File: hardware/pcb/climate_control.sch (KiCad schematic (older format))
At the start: 36 parts, among them J1 Switch, J2 BatteryIn, J3 USB_C, J4 HeatElement, J5 ICSP, Q2 NTR3C21NZ, U1 TP4056, U2 XB8089A, U3 ATmega328PB-AU, U4 TPS61230DRC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

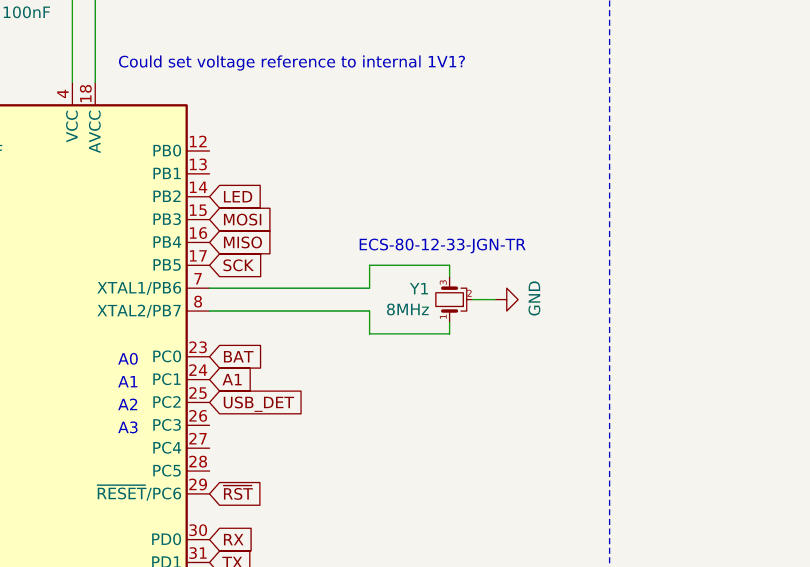
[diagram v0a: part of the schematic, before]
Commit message: Removed crystal.
The ATMega does not need an external crystal. Now removed.
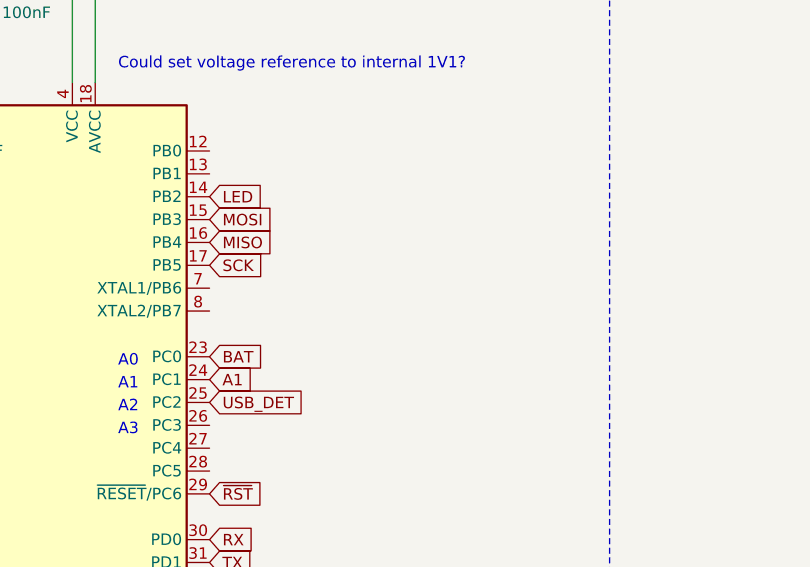
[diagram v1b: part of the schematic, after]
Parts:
- removed Y1: 8MHz, climate_control:ECX-32, symbol Device:Crystal_GND2_Small
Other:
- note removed: "ECS-80-12-33-JGN-TR"
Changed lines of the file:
@@
 SWITCH
 $Comp
-L Device:Crystal_GND2_Small Y1
-U 1 1 6050B57C
-P 6750 7500
-F 0 "Y1" V 6796 7588 50  0000 L CNN
-F 1 "8MHz" V 6705 7588 50  0000 L CNN
-F 2 "climate_control:ECX-32" H 6750 7500 50  0001 C CNN
-F 3 "~" H 6750 7500 50  0001 C CNN
-	1    6750 7500
-	0    -1   -1   0
-$EndComp
-Wire Wire Line
-	5700 7450 6400 7450
-Wire Wire Line
-	6400 7450 6400 7350
-Wire Wire Line
-	6400 7350 6750 7350
-Wire Wire Line
-	6750 7350 6750 7400
-Wire Wire Line
-	5700 7550 6400 7550
-Wire Wire Line
-	6400 7650 6750 7650
-Wire Wire Line
-	6750 7650 6750 7600
-Wire Wire Line
-	6400 7550 6400 7650
-$Comp
-L power:GND #PWR0133
-U 1 1 60524C00
-P 6950 7500
-F 0 "#PWR0133" H 6950 7250 50  0001 C CNN
-F 1 "GND" H 6955 7327 50  0000 C CNN
-F 2 "" H 6950 7500 50  0001 C CNN
-F 3 "" H 6950 7500 50  0001 C CNN
-	1    6950 7500
-	0    -1   -1   0
-$EndComp
-Wire Wire Line
-	6950 7500 6850 7500
-$Comp
 L Connector:Screw_Terminal_01x04 J1
 U 1 1 6052D28F
@@
 Wire Wire Line
 	8200 1700 8200 1750
-Text Notes 6350 7300 0    50   ~ 0
-ECS-80-12-33-JGN-TR
 Text GLabel 6450 9700 0    50   Input ~ 0
 MISO
